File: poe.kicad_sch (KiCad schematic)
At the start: 59 parts, among them IC1 TPS2378DDA, J1 B2B-XH-A_LF__SN_, J6 SS-74800-144, U3 TPS2373-3RGW, U4 URB4805YMD-30WR3

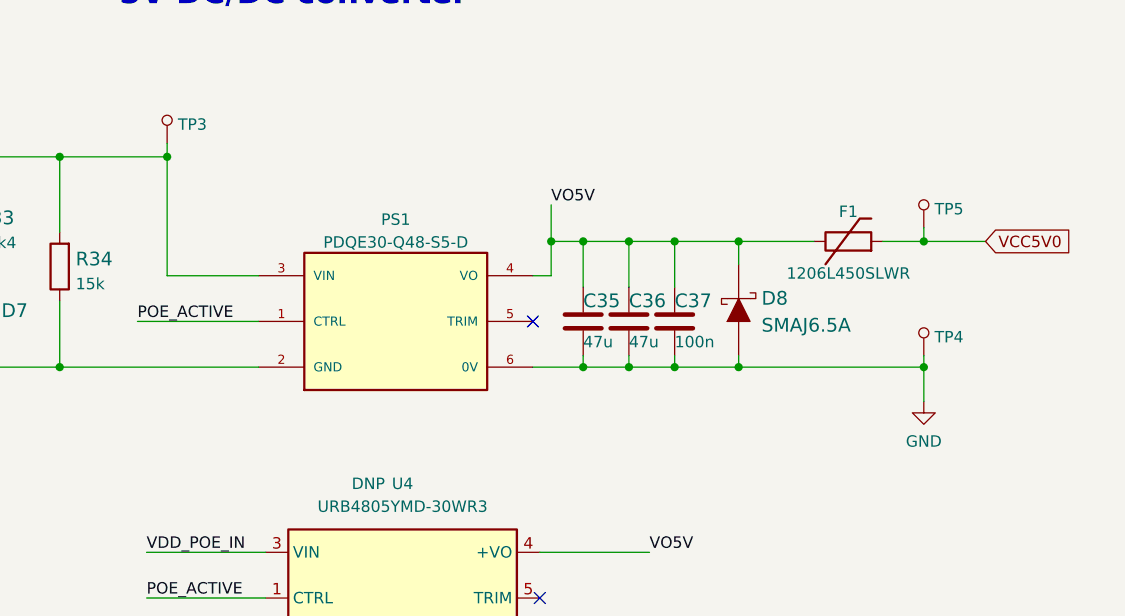
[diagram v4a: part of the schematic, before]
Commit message: Update PDQE30-Q48-S5-D symbol and footprint
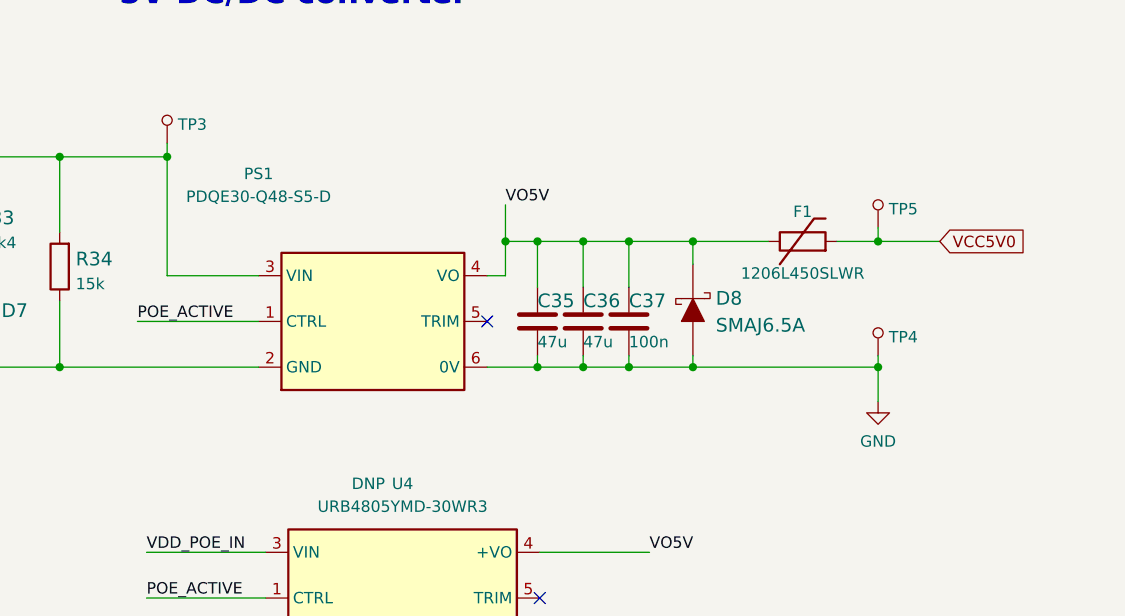
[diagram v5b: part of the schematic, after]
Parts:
- PS1: footprint scalenode-cm4-baseboard-footprints:PDQE30-Q48 -> antmicro-footprints:PDQE30-Q48; symbol scalenode-cm4-baseboard:PDQE30-Q48-S5-D -> antmicroDCDCConverters:PDQE30-Q48-S5-D; Author (none) -> Antmicro; License (none) -> Apache-2.0; Manufacturer CUI -> CUI Inc; STANDARD (none) -> Manufacturer Recommendations
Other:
- moved on the sheet: C35, C36, C37, D8, F1, PS1, TP4, TP5

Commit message: Update URB4805YMD-30WR3 symbol and footprint
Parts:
- U4: footprint scalenode-cm4-baseboard-footprints:URB4805YMD-30WR3 -> antmicro-footprints:URB4805YMD-30WR3; symbol scalenode-cm4-baseboard:URB4805YMD-30WR3 -> antmicroDCDCConverters:URB4805YMD-30WR3; Author (none) -> Antmicro; License Apache-2.0 License -> Apache-2.0
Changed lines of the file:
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@@
     (pin "2")
   )
-  (symbol (lib_id "scalenode-cm4-baseboard:URB4805YMD-30WR3") (at 277.368 220.98 0) (unit 1)
+  (symbol (lib_id "antmicroDCDCConverters:URB4805YMD-30WR3") (at 277.368 220.98 0) (unit 1)
     (in_bom yes) (on_board yes)
     (property "Reference" "U4" (id 0) (at 292.608 213.36 0))
     (property "Value" "URB4805YMD-30WR3" (id 1) (at 292.608 215.9 0))
-    (property "Footprint" "scalenode-cm4-baseboard-footprints:URB4805YMD-30WR3" (id 2) (at 291.338 212.09 0)
+    (property "Footprint" "antmicro-footprints:URB4805YMD-30WR3" (id 2) (at 291.338 212.09 0)
       (effects (font (size 1.27 1.27)) (justify bottom) hide)
     )
@@
       (effects (font (size 1.27 1.27)) hide)
     )
-    (property "License" "Apache-2.0 License" (id 6) (at 291.338 213.36 0)
+    (property "License" "Apache-2.0" (id 6) (at 291.338 213.36 0)
       (effects (font (size 1.27 1.27)) hide)
     )
@@
     )
     (property "DNP" "DNP" (id 8) (at 288.798 213.36 0))
+    (property "Author" "Antmicro" (id 9) (at 291.338 208.28 0)
+      (effects (font (size 1.27 1.27)) hide)
+    )
     (pin "1")
     (pin "2")

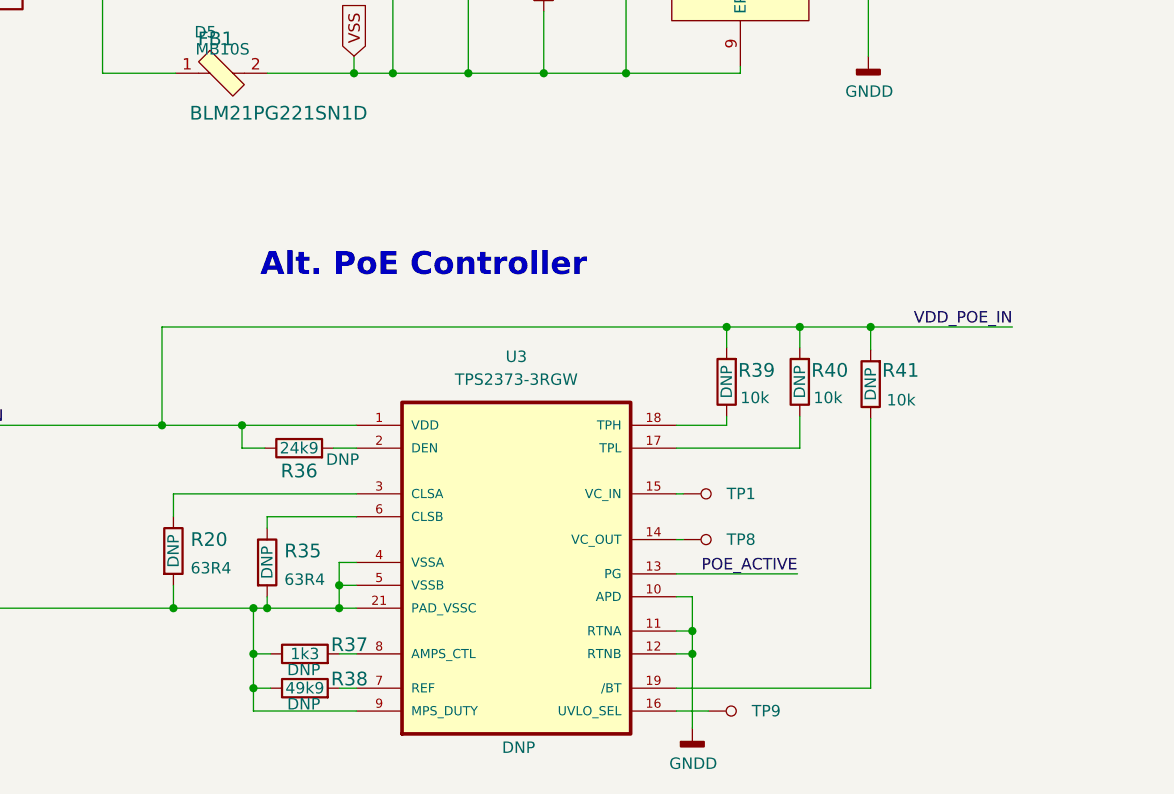
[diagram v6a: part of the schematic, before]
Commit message: Update TPS2373-3RGW symbol and QFN65P500X500X100-21N footprint
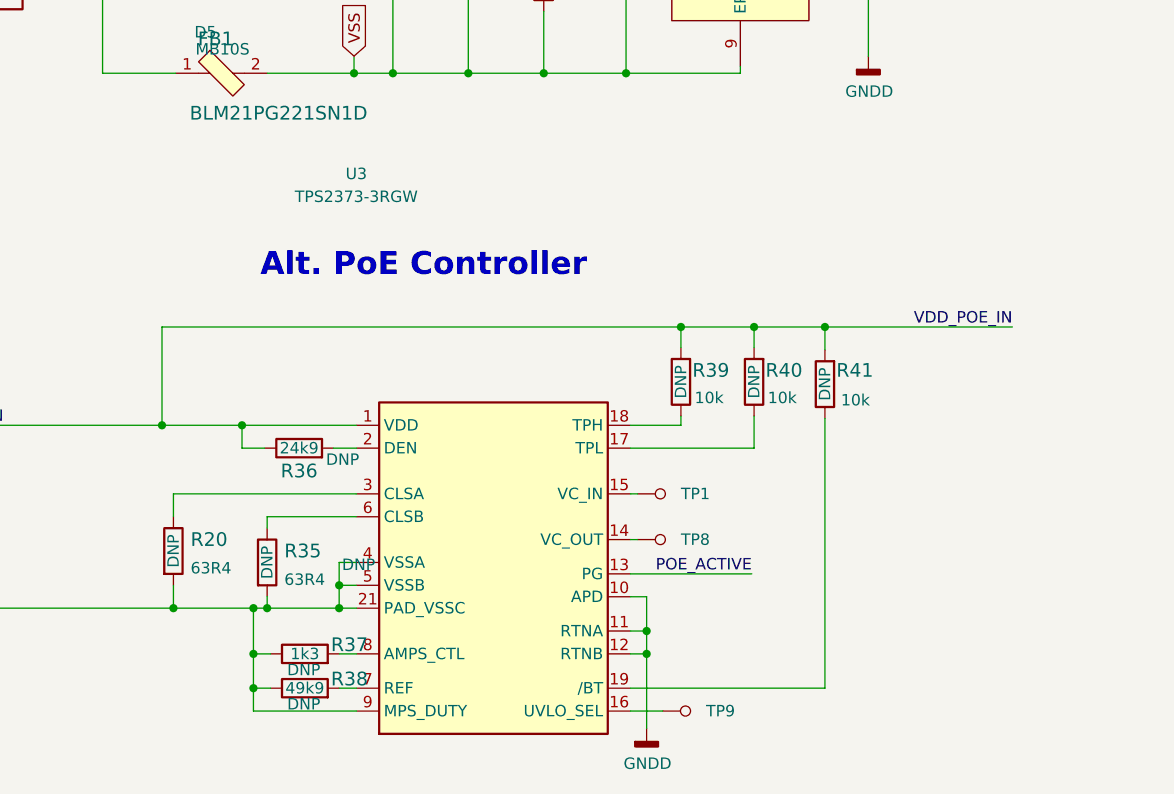
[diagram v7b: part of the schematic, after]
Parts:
- U3: footprint scalenode-cm4-baseboard-footprints:QFN65P500X500X100-21N -> antmicro-footprints:SOT-583; symbol scalenode-cm4-baseboard:TPS2373-3RGW -> antmicroPMICPowerDistributionSwitchesLoadDrivers:TPS2373-3RGW; Author (none) -> Antmicro; License (none) -> Apache-2.0; now in the parts list
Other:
- moved on the sheet: R39, R40, R41, TP1, TP8, TP9, U3

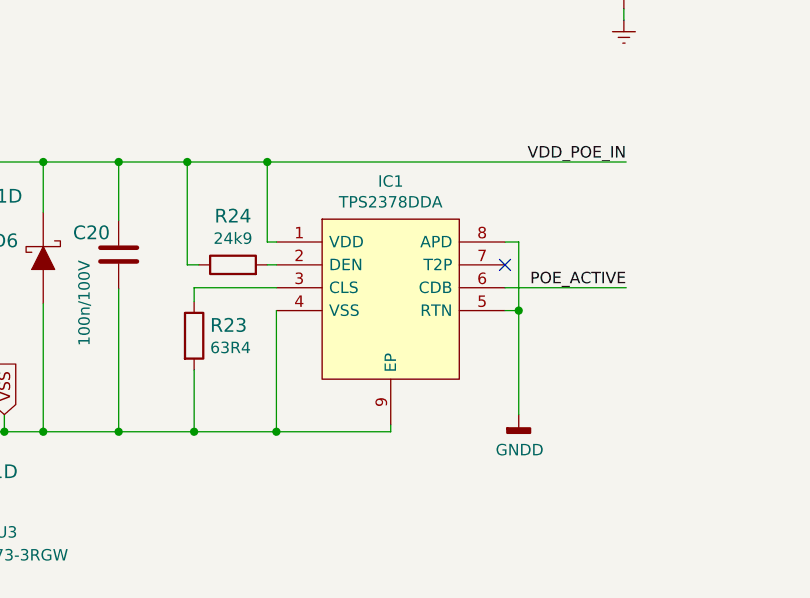
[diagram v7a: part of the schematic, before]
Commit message: Update TPS2378DDA symbol and SOIC127P600X170-9N footprint
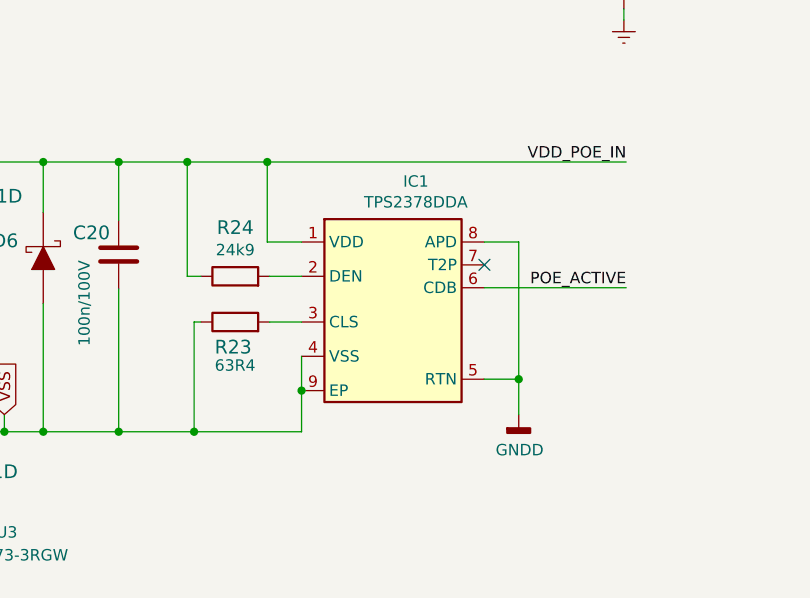
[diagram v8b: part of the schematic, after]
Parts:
- IC1: footprint scalenode-cm4-baseboard-footprints:SOIC127P600X170-9N -> antmicro-footprints:VQFN-20_5x5x1mm_P0.65mm; symbol scalenode-cm4-baseboard:TPS2378DDA -> antmicroPMICPowerDistributionSwitchesLoadDrivers:TPS2378DDA; Author (none) -> Antmicro; License (none) -> Apache-2.0
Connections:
- net VSS: now also R23.1; no longer R23.2
- net at IC1.3 (CLS): now also R23.2; no longer R23.1
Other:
- moved on the sheet: IC1, R23, R24
